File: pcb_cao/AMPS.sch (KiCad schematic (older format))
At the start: 17 parts, among them J1 Conn_01x02, J10 Conn_01x02, J11 Conn_01x02, J12 Conn_01x16, J2 Conn_01x02, J3 Conn_01x02, J4 Conn_01x02, J5 Conn_01x03, J6 Conn_01x03, J7 Conn_01x03, J8 Conn_01x03, U1 ARDUINO_MICRO_SHIELD

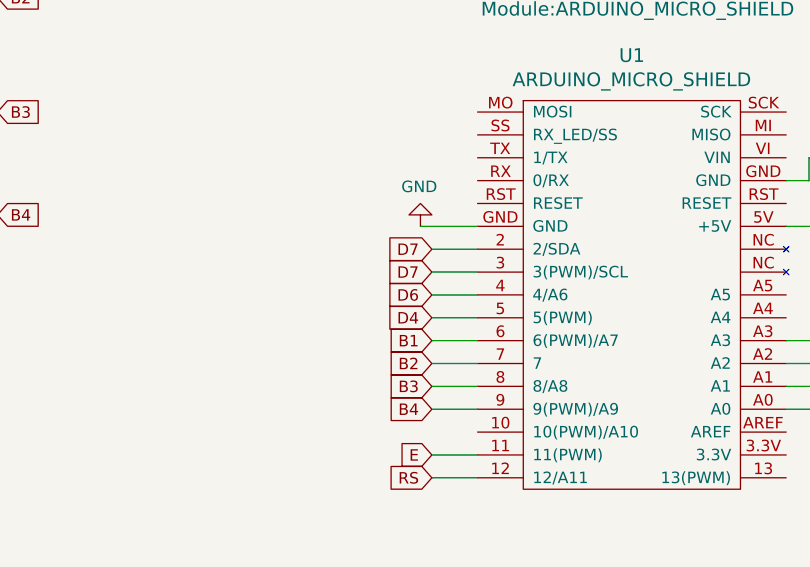
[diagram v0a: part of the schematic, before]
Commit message: Fix routing problems
 - Duplicate pins tag on the LCD connexion
 - Fix Footprints references
 - Increase vias diameter
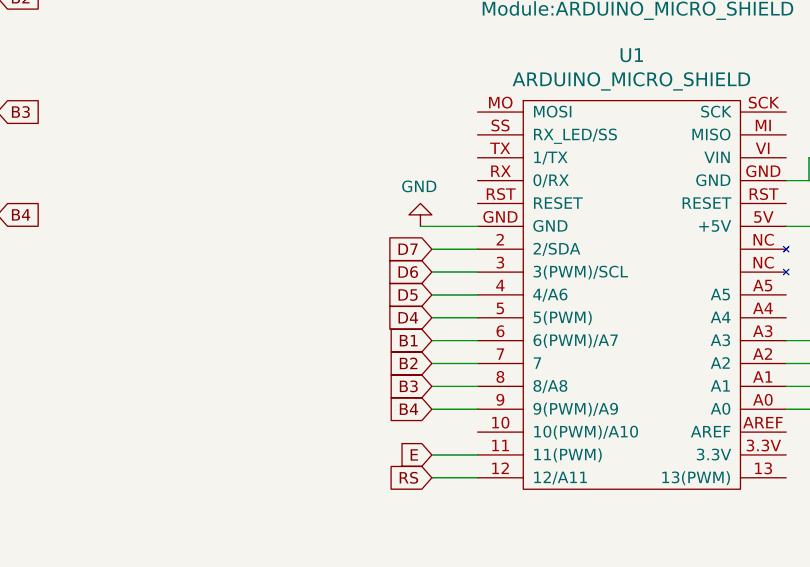
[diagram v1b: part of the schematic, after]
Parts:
- J1, J10, J11, J2, J3, J4: footprint TerminalBlock_TE-Connectivity:TerminalBlock_TE_292207-2_1x02_P1.5mm_Horizontal -> Connector_PinHeader_2.54mm:PinHeader_1x02_P2.54mm_Vertical
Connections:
- net D5: now also U1.4 (4/A6)
- net D6: now also U1.3 (3(PWM)/SCL); no longer U1.4 (4/A6)
- net D7: no longer U1.3 (3(PWM)/SCL)
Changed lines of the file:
@@
 F 0 "J2" H 1370 2025 50  0000 C CNN
 F 1 "Conn_01x02" H 1370 2116 50  0000 C CNN
-F 2 "TerminalBlock_TE-Connectivity:TerminalBlock_TE_292207-2_1x02_P1.5mm_Horizontal" H 1450 2350 50  0001 C CNN
+F 2 "Connector_PinHeader_2.54mm:PinHeader_1x02_P2.54mm_Vertical" H 1450 2350 50  0001 C CNN
 F 3 "~" H 1450 2350 50  0001 C CNN
 	1    1450 2350
@@
 F 0 "J3" H 1370 2525 50  0000 C CNN
 F 1 "Conn_01x02" H 1370 2616 50  0000 C CNN
-F 2 "TerminalBlock_TE-Connectivity:TerminalBlock_TE_292207-2_1x02_P1.5mm_Horizontal" H 1450 2850 50  0001 C CNN
+F 2 "Connector_PinHeader_2.54mm:PinHeader_1x02_P2.54mm_Vertical" H 1450 2850 50  0001 C CNN
 F 3 "~" H 1450 2850 50  0001 C CNN
 	1    1450 2850
@@
 F 0 "J1" H 1370 1575 50  0000 C CNN
 F 1 "Conn_01x02" H 1370 1666 50  0000 C CNN
-F 2 "TerminalBlock_TE-Connectivity:TerminalBlock_TE_292207-2_1x02_P1.5mm_Horizontal" H 1450 1900 50  0001 C CNN
+F 2 "Connector_PinHeader_2.54mm:PinHeader_1x02_P2.54mm_Vertical" H 1450 1900 50  0001 C CNN
 F 3 "~" H 1450 1900 50  0001 C CNN
 	1    1450 1900
@@
 F 0 "J4" H 1370 2975 50  0000 C CNN
 F 1 "Conn_01x02" H 1370 3066 50  0000 C CNN
-F 2 "TerminalBlock_TE-Connectivity:TerminalBlock_TE_292207-2_1x02_P1.5mm_Horizontal" H 1450 3300 50  0001 C CNN
+F 2 "Connector_PinHeader_2.54mm:PinHeader_1x02_P2.54mm_Vertical" H 1450 3300 50  0001 C CNN
 F 3 "~" H 1450 3300 50  0001 C CNN
 	1    1450 3300
@@
 F 0 "J10" H 4980 5392 50  0000 L CNN
 F 1 "Conn_01x02" H 4980 5301 50  0000 L CNN
-F 2 "TerminalBlock_TE-Connectivity:TerminalBlock_TE_292207-2_1x02_P1.5mm_Horizontal" H 4900 5400 50  0001 C CNN
+F 2 "Connector_PinHeader_2.54mm:PinHeader_1x02_P2.54mm_Vertical" H 4900 5400 50  0001 C CNN
 F 3 "~" H 4900 5400 50  0001 C CNN
 	1    4900 5400
@@
 D4
 Text GLabel 4550 3650 0    50   Input ~ 0
+D5
+Text GLabel 4550 3550 0    50   Input ~ 0
 D6
-Text GLabel 4550 3550 0    50   Input ~ 0
-D7
 Text GLabel 4550 3450 0    50   Input ~ 0
 D7
@@
 F 0 "J11" H 4980 6092 50  0000 L CNN
 F 1 "Conn_01x02" H 4980 6001 50  0000 L CNN
-F 2 "TerminalBlock_TE-Connectivity:TerminalBlock_TE_292207-2_1x02_P1.5mm_Horizontal" H 4900 6100 50  0001 C CNN
+F 2 "Connector_PinHeader_2.54mm:PinHeader_1x02_P2.54mm_Vertical" H 4900 6100 50  0001 C CNN
 F 3 "~" H 4900 6100 50  0001 C CNN
 	1    4900 6100

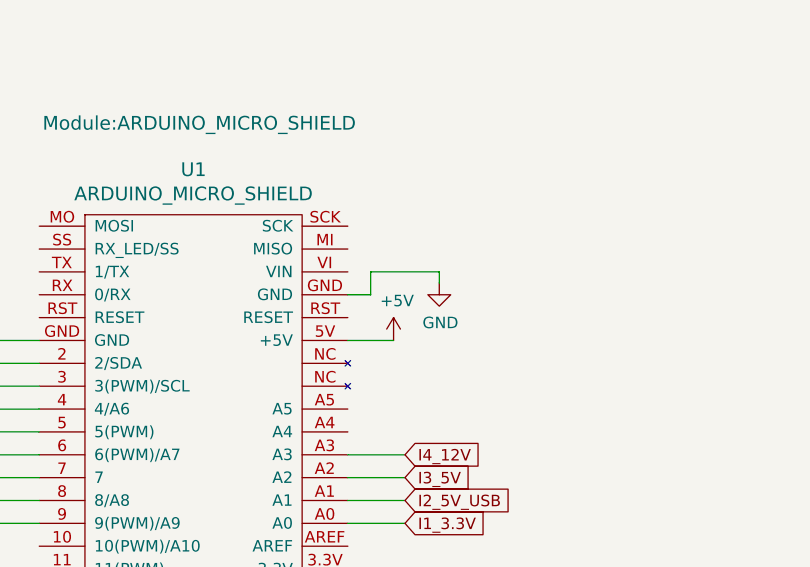
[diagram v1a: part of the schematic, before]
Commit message: Power the arduino micro by pin 'Vin' not pin '5V'
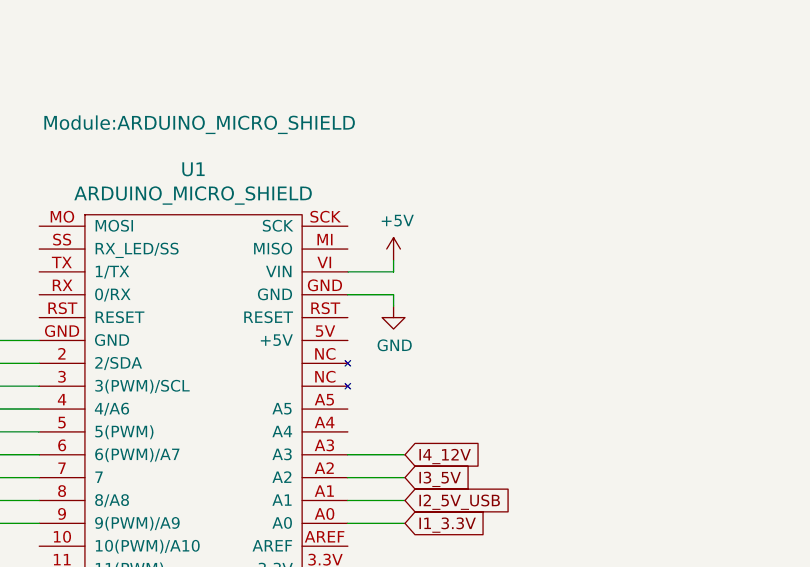
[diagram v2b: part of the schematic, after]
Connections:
- net +5V: now also U1.VI (VIN); no longer U1.5V (+5V)
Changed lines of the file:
@@
 L power:+5V #PWR0102
 U 1 1 5C3B8514
-P 6300 3350
-F 0 "#PWR0102" H 6300 3200 50  0001 C CNN
-F 1 "+5V" H 6315 3523 50  0000 C CNN
-F 2 "" H 6300 3350 50  0001 C CNN
-F 3 "" H 6300 3350 50  0001 C CNN
-	1    6300 3350
+P 6300 3000
+F 0 "#PWR0102" H 6300 2850 50  0001 C CNN
+F 1 "+5V" H 6315 3173 50  0000 C CNN
+F 2 "" H 6300 3000 50  0001 C CNN
+F 3 "" H 6300 3000 50  0001 C CNN
+	1    6300 3000
 	1    0    0    -1
 $EndComp
@@
 L power:GND #PWR0103
 U 1 1 5C3B85F7
-P 6500 3100
-F 0 "#PWR0103" H 6500 2850 50  0001 C CNN
-F 1 "GND" H 6505 2927 50  0000 C CNN
-F 2 "" H 6500 3100 50  0001 C CNN
-F 3 "" H 6500 3100 50  0001 C CNN
-	1    6500 3100
-	1    0    0    -1
-$EndComp
-Wire Wire Line
-	6100 3150 6200 3150
-Wire Wire Line
-	6200 3150 6200 3050
-Wire Wire Line
-	6200 3050 6500 3050
-Wire Wire Line
-	6500 3050 6500 3100
-Wire Wire Line
-	6100 3350 6300 3350
+P 6300 3200
+F 0 "#PWR0103" H 6300 2950 50  0001 C CNN
+F 1 "GND" H 6305 3027 50  0000 C CNN
+F 2 "" H 6300 3200 50  0001 C CNN
+F 3 "" H 6300 3200 50  0001 C CNN
+	1    6300 3200
+	1    0    0    -1
+$EndComp
 Text GLabel 6350 4150 2    50   Input ~ 0
 I1_3.3V
@@
 	1650 3300 2400 3300
 Connection ~ 2400 3300
+Wire Wire Line
+	6300 3150 6300 3200
+Wire Wire Line
+	6100 3150 6300 3150
+Wire Wire Line
+	6100 3050 6300 3050
+Wire Wire Line
+	6300 3050 6300 3000
 $EndSCHEMATC

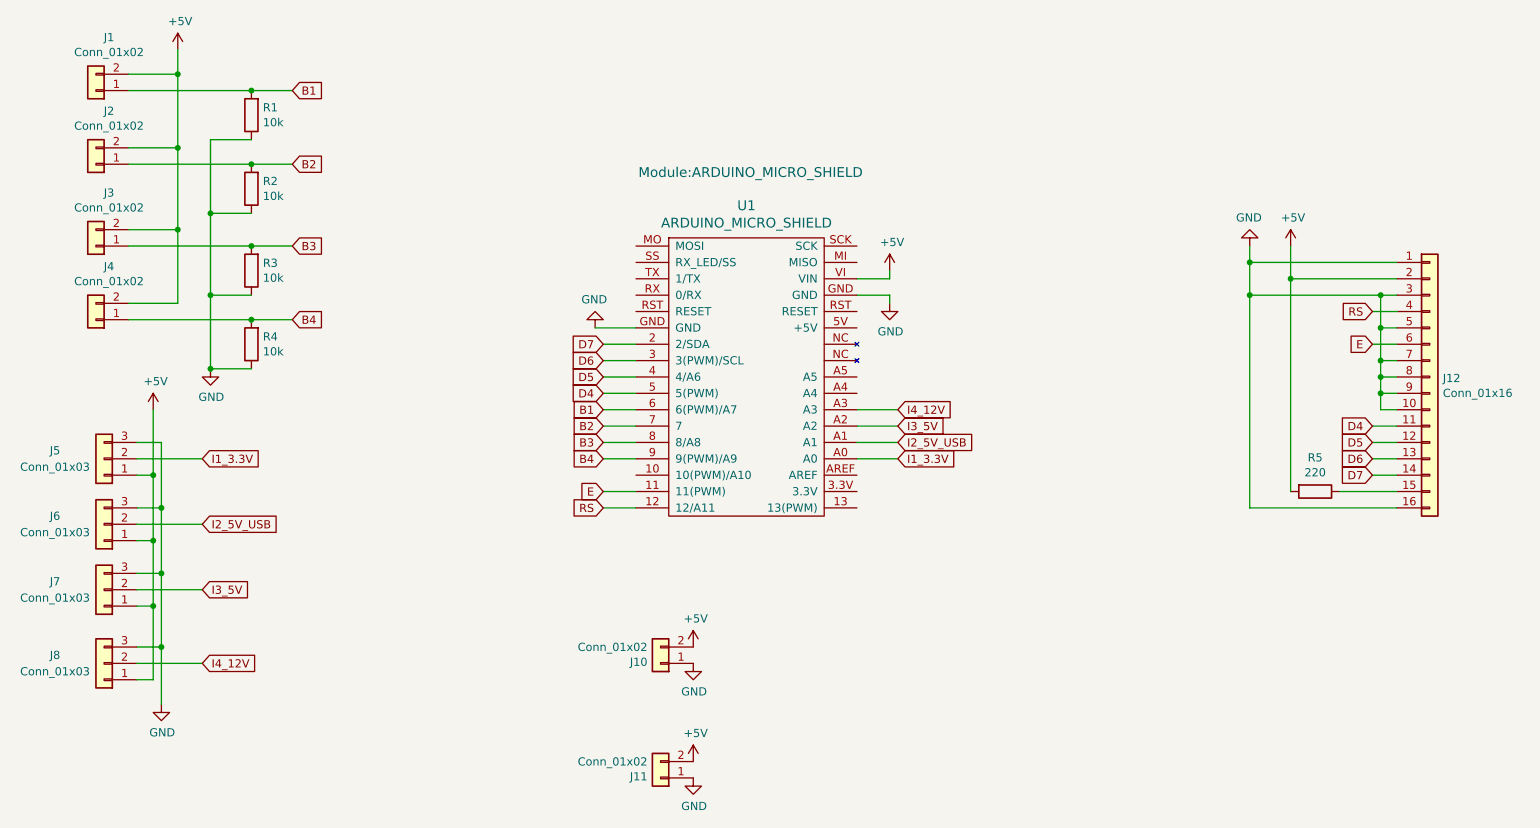
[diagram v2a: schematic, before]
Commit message: Redesign of the PCB
Use a I2C LCD screen
Use only 2 buttons
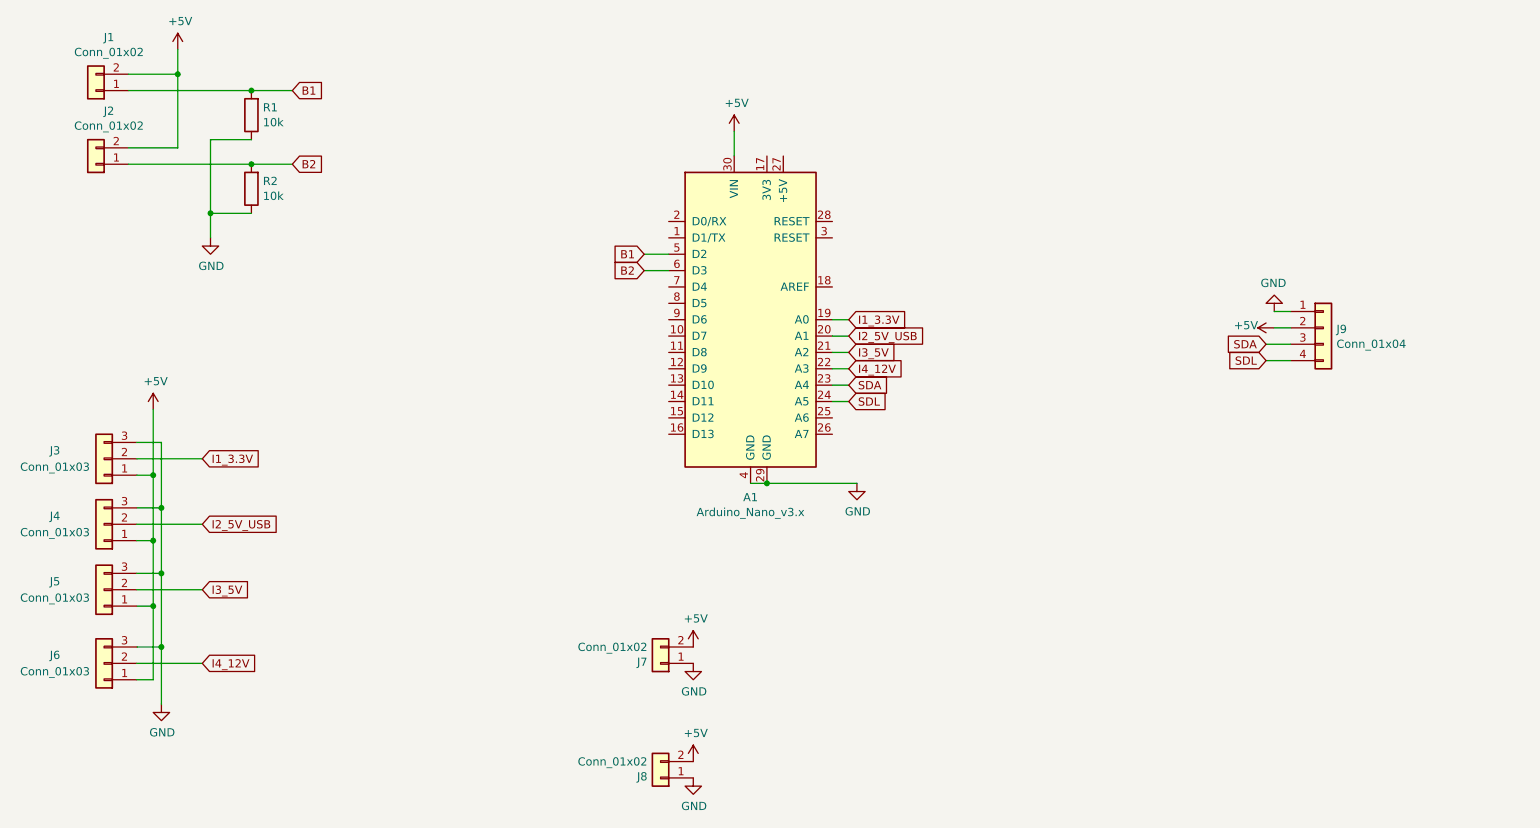
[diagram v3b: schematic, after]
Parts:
- removed J12: Conn_01x16, Connector_PinHeader_2.54mm:PinHeader_1x16_P2.54mm_Vertical, symbol Connector_Generic:Conn_01x16
- removed J3, J4: Conn_01x02, Connector_PinHeader_2.54mm:PinHeader_1x02_P2.54mm_Vertical, symbol Connector_Generic:Conn_01x02
- removed R3, R4: 10k, Resistor_THT:R_Axial_DIN0207_L6.3mm_D2.5mm_P10.16mm_Horizontal, symbol Device:R
- removed R5: 220, Resistor_THT:R_Axial_DIN0207_L6.3mm_D2.5mm_P10.16mm_Horizontal, symbol Device:R
- removed U1: ARDUINO_MICRO_SHIELD, Module:ARDUINO_MICRO_SHIELD, symbol AMPS-rescue:ARDUINO_MICRO_SHIELD-Arduino_Micro
- added A1: Arduino_Nano_v3.x, Module:Arduino_Nano, symbol MCU_Module:Arduino_Nano_v3.x
- added J9: Conn_01x04, Connector_PinHeader_2.54mm:PinHeader_1x04_P2.54mm_Vertical, symbol Connector_Generic:Conn_01x04
- renumbered J5 to J3, J6 to J4, J7 to J5, J8 to J6, J10 to J7, J11 to J8
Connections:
- net +5V: now also A1.30 (VIN), J9.2 (Pin_2)
- net B1: now also A1.5 (D2)
- net B2: now also A1.6 (D3)
- net GND: now also A1.29 (GND), A1.4 (GND), J9.1 (Pin_1)
- net I1_3.3V: now also A1.19 (A0)
- net I2_5V_USB: now also A1.20 (A1)
- net I3_5V: now also A1.21 (A2)
- net I4_12V: now also A1.22 (A3)
- new net SDA: A1.23 (A4), J9.3 (Pin_3)
- new net SDL: A1.24 (A5), J9.4 (Pin_4)
